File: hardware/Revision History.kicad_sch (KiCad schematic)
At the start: 0 parts

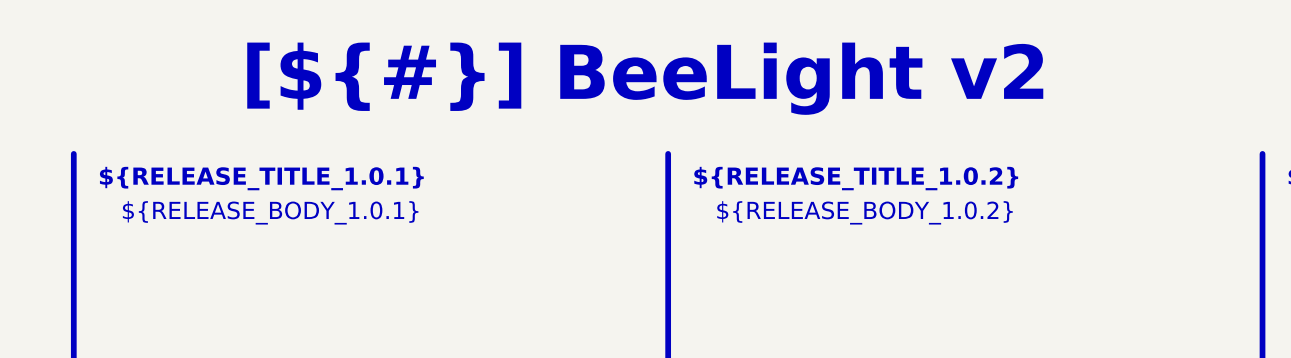
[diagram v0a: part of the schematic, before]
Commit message: Implement new CI/CD workflow
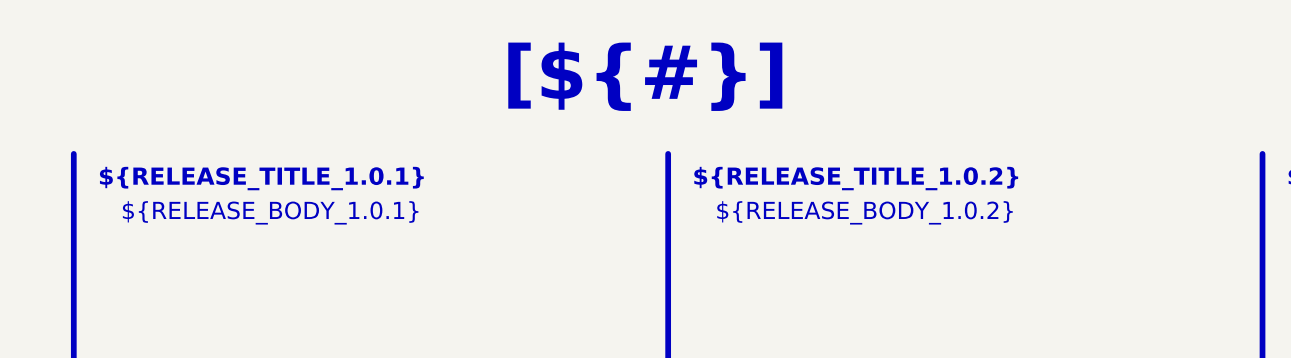
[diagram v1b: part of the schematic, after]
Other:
- title: BeeLight v2 -> (none)
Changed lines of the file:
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@@
 	(paper "A4")
 	(title_block
-		(title "BeeLight v2")
 		(date "2025-06-05")
 		(rev "${REVISION}")

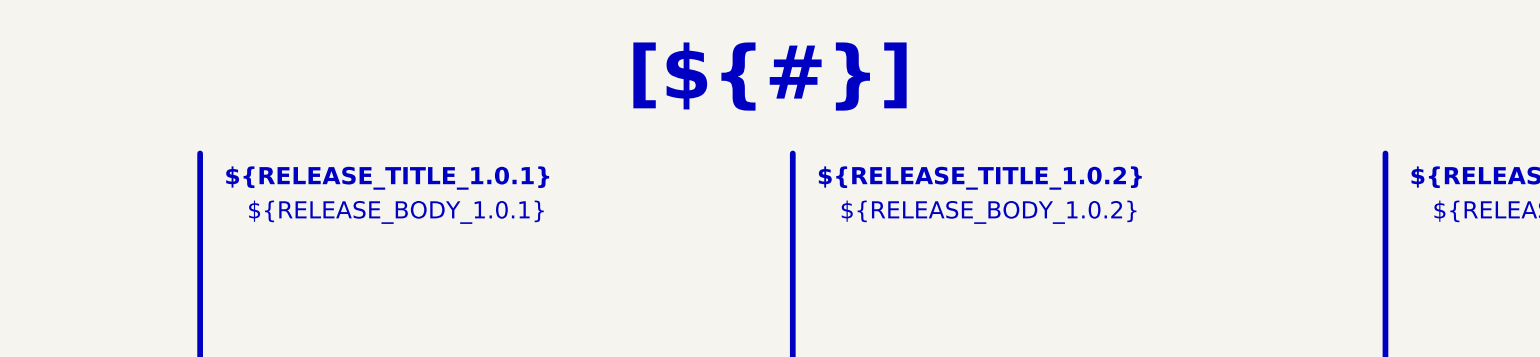
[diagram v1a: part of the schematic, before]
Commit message: - Change ADC filter capacitor to 1 nF - Update documentation with current consumption - Update CI/CD pipeline
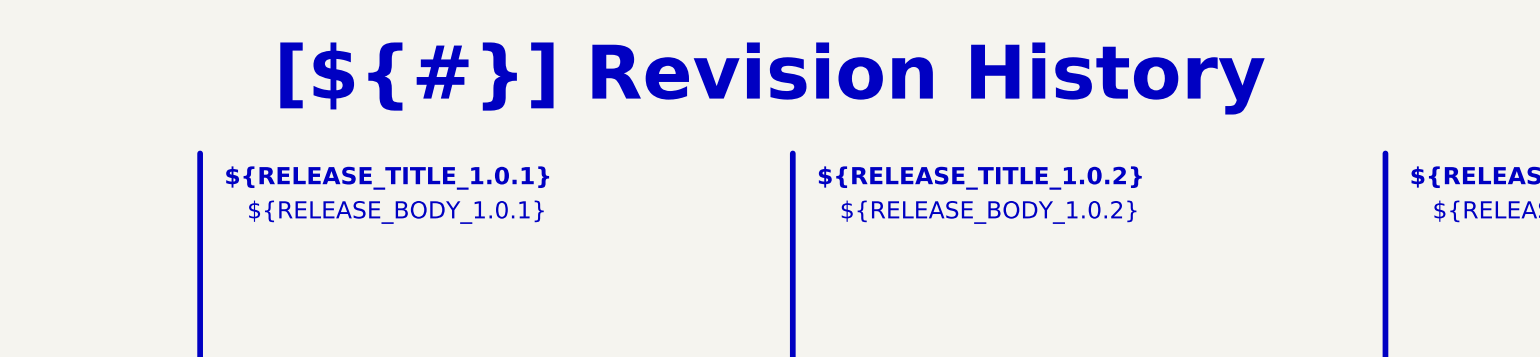
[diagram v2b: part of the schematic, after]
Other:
- title: (none) -> Revision History
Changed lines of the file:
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@@
 	(paper "A4")
 	(title_block
+		(title "Revision History")
 		(date "2025-06-05")
 		(rev "${REVISION}")
